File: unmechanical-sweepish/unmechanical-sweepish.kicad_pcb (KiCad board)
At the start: 4 copper layers, 214 x 145.5 mm, 168 parts, among them J1 HytePro M, J2 USB_C_Receptacle_USB2.0, J3 M, J4 HytePro F, J5 USB_C_Receptacle_USB2.0, J6 M, Q1 AO3400A, Q2 AO3400A, SW1 B/R, SW2 B/R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

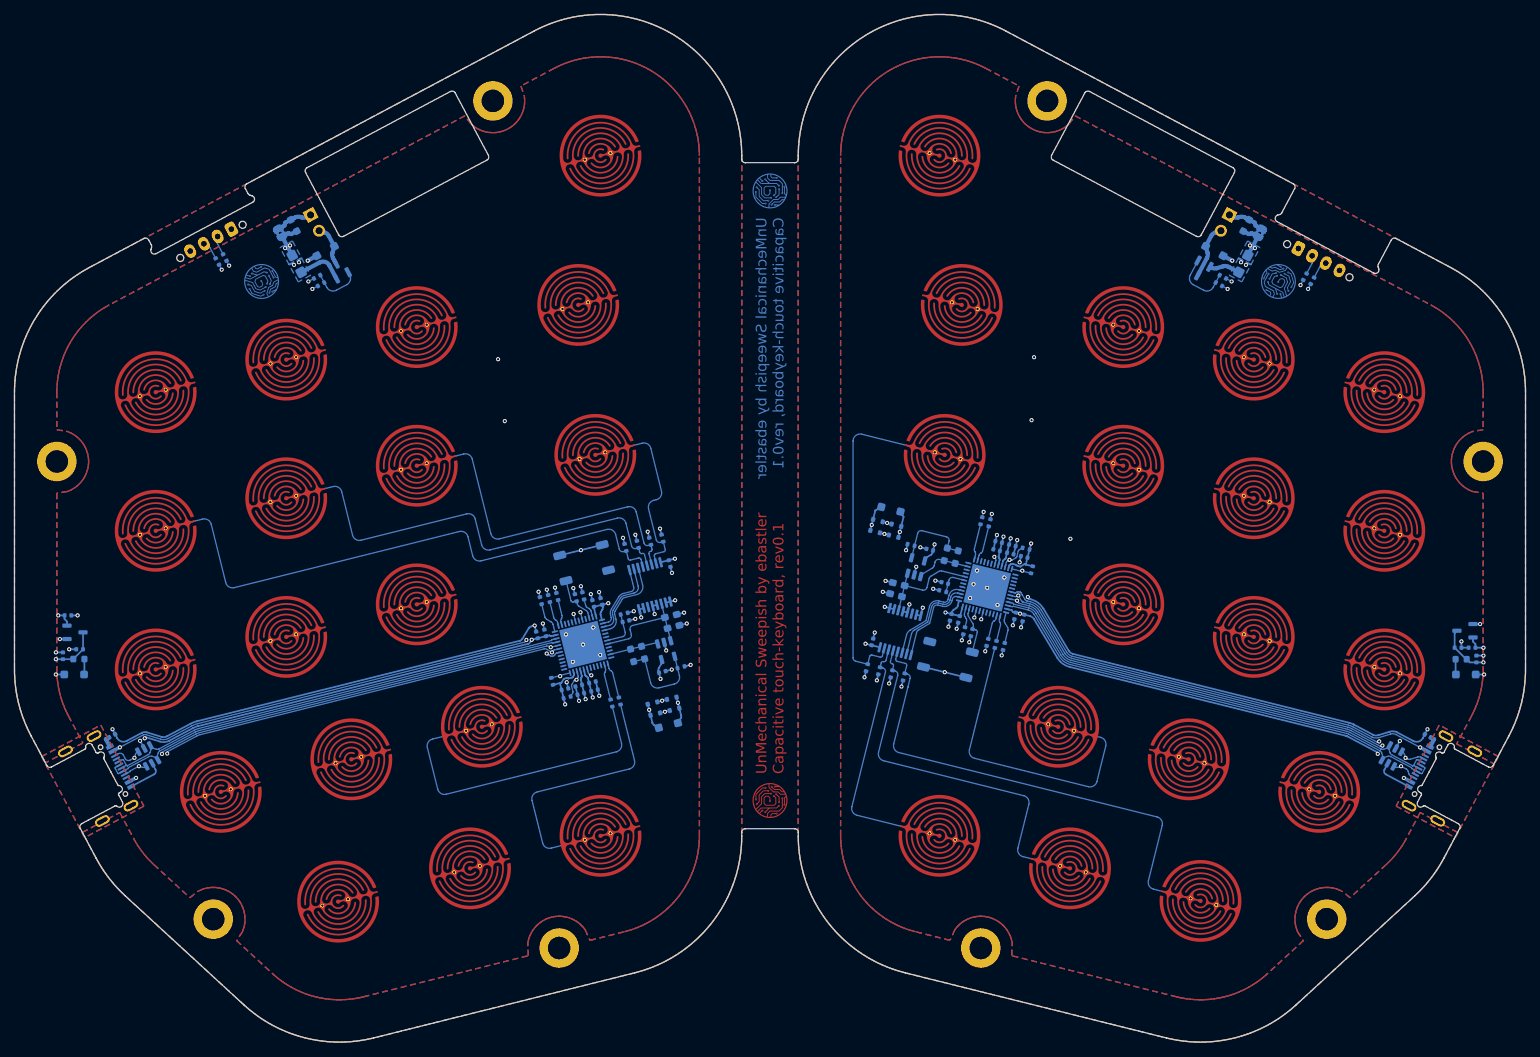
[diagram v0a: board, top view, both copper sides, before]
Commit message: update to kicad 8 model paths
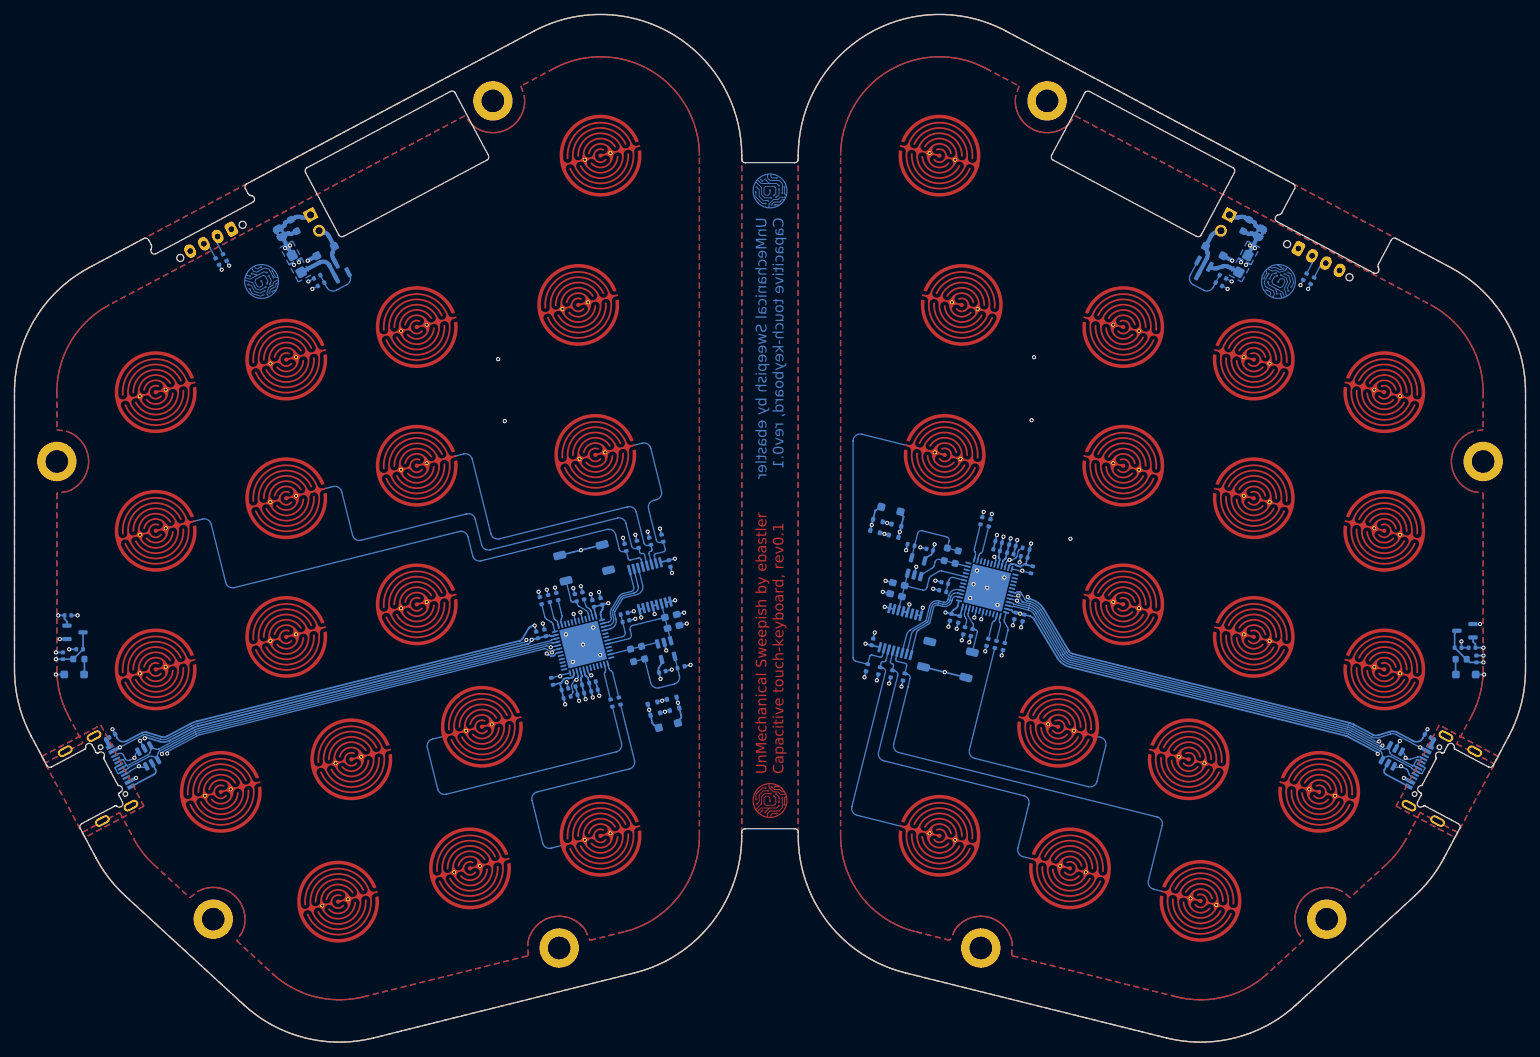
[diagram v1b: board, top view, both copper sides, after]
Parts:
- J1: footprint PCM_marbastlib-xp-various:CON_HytePro_M411P_Plug_1x04-P2.20mm_Horizontal_FlushMount -> PCM_marbastlib-various:CON_HytePro_M411P_Plug_1x04-P2.20mm_Horizontal_FlushMount
- J4: footprint PCM_marbastlib-xp-various:CON_HytePro_M411P_Receptacle_1x04-P2.20mm_Horizontal_FlushMount -> PCM_marbastlib-various:CON_HytePro_M411P_Receptacle_1x04-P2.20mm_Horizontal_FlushMount
- L1, L2: value BLM15PX121SN1D -> BLM15PX121SN1D

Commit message: remove outdated graphics on user.drawings as reported in #2
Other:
- board text removed: "PCB Edge"
